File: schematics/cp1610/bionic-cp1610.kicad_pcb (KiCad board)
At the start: 2 copper layers, 25.4 x 68.6 mm, 33 parts, among them J1 Bionic-P135, J2 Bionic-P245, U1 CP1610, U2 11AA010-I/TT, U3 UCC27324, U4 74LVC1G02, U5 74LVC1G06, U6 LM2776, U7 TPS72301, U8 NJW4132

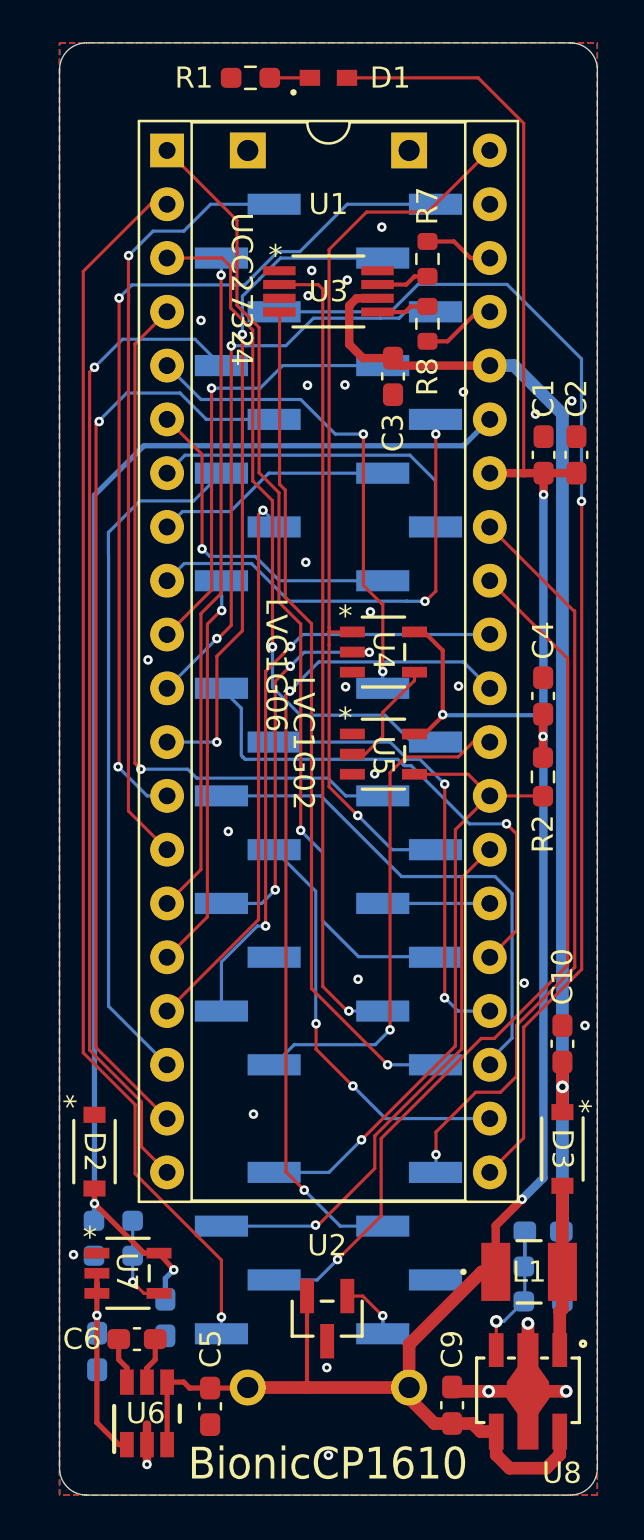
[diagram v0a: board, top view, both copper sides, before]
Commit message: [schematics] Straighten board tracks and regenerate Gerbers
straighten_tracks.py on every routed board: router leftovers snapped to
0/45/90 degrees and redundant segments merged, each pass DRC-checked
(counts unchanged). Gerbers and drill files of the changed boards are
regenerated with each board's plot settings, keeping the committed file
sets; tms9980 keeps its tracks (the rebuild left a dangling VCC stub).
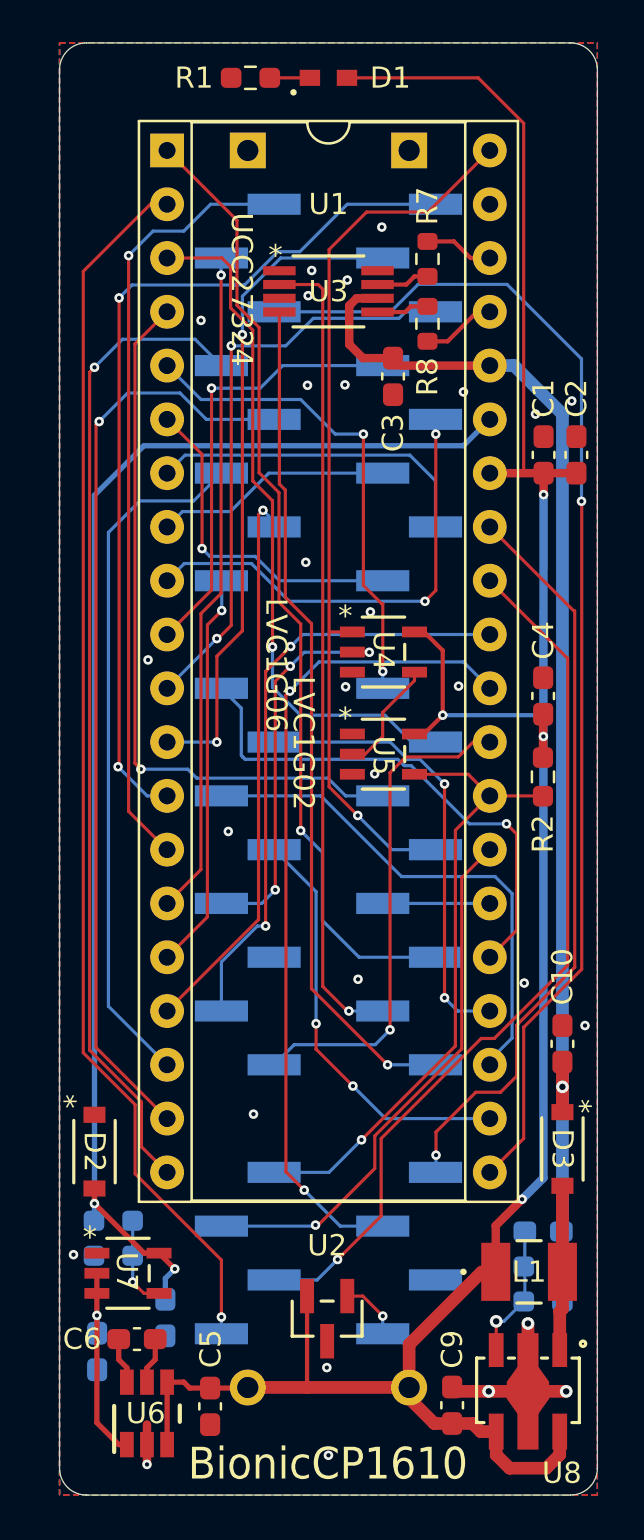
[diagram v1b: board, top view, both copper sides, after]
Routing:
- net VDD: track 59.7 -> 56.9 mm
- net VCC: track 119.2 -> 117.1 mm
- net Net-(U8-IN-): track 8.09 -> 6.35 mm
- net Net-(D3-A): track 9.41 -> 7.75 mm
- net BC1: track 32.6 -> 31.5 mm
- net ~{BUSACK}: track 23.6 -> 22.8 mm
- net ~{MSYNC}: track 58.1 -> 57.4 mm
- net Net-(U1-Φ2): track 3.52 -> 2.92 mm
- net Net-(J2-P57): track 3.50 -> 2.90 mm

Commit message: [schematics] Align silkscreen reference labels
align_silk.py snaps each footprint kind's labels onto their common
offset and angle and clears labels DRC flags on silkscreen; 76 labels on
22 boards, no DRC count grows. Their Gerbers are regenerated.
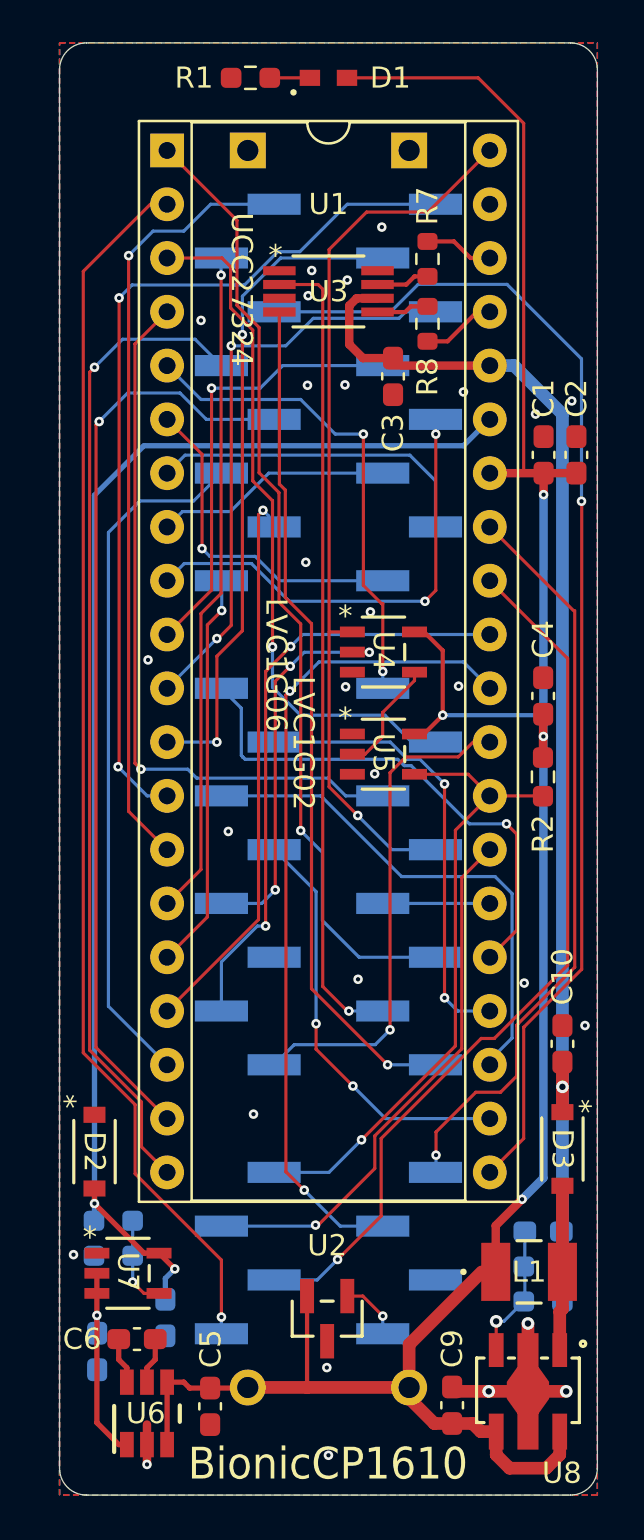
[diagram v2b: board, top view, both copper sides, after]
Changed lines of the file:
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@@
 		(tags "capacitor handsolder")
 		(property "Reference" "C9"
-			(at 2.6405 0 90)
+			(at 2.67 0 90)
 			(layer "F.SilkS")
 			(effects
@@
 		(tags "SN74LVC1G06DBVT ")
 		(property "Reference" "U5"
-			(at 0 0.061001 270)
+			(at 0 -0.07 270)
 			(unlocked yes)
 			(layer "F.SilkS")
@@
 		(tags "SN74LVC1G06DBVT ")
 		(property "Reference" "U7"
-			(at -0.05715 -0.065999 270)
+			(at 0 -0.07 270)
 			(unlocked yes)
 			(layer "F.SilkS")
@@
 		(tags "capacitor handsolder")
 		(property "Reference" "C4"
-			(at 2.6225 0.01 90)
+			(at 2.67 0 90)
 			(layer "F.SilkS")
 			(effects
@@
 		(tags "capacitor handsolder")
 		(property "Reference" "C7"
-			(at 2.7686 0 90)
+			(at 2.96 0 90)
 			(layer "B.SilkS")
 			(effects
@@
 		(tags "capacitor handsolder")
 		(property "Reference" "C8"
-			(at 3.1636 -0.0028 90)
+			(at 2.96 0 90)
 			(layer "B.SilkS")
 			(effects
